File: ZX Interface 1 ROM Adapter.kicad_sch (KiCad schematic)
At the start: 4 parts, among them J1 Conn_01x08_Socket, J2 24DIL Socket, J3 Conn_01x16, J4 Conn_01x16

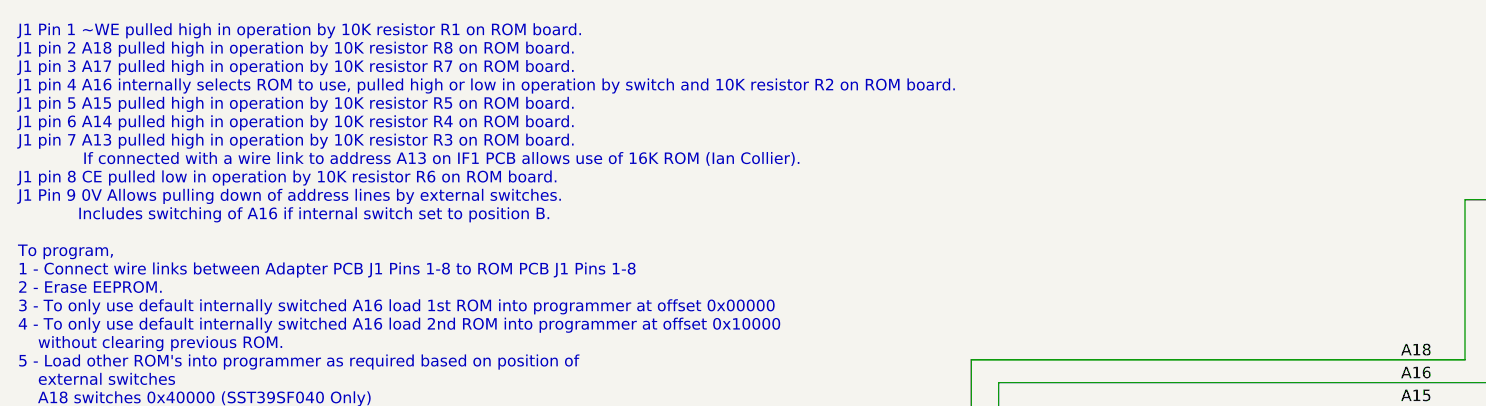
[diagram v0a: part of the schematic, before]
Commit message: Updated to use 8 Pin Right Angled Single-In-Line Connector
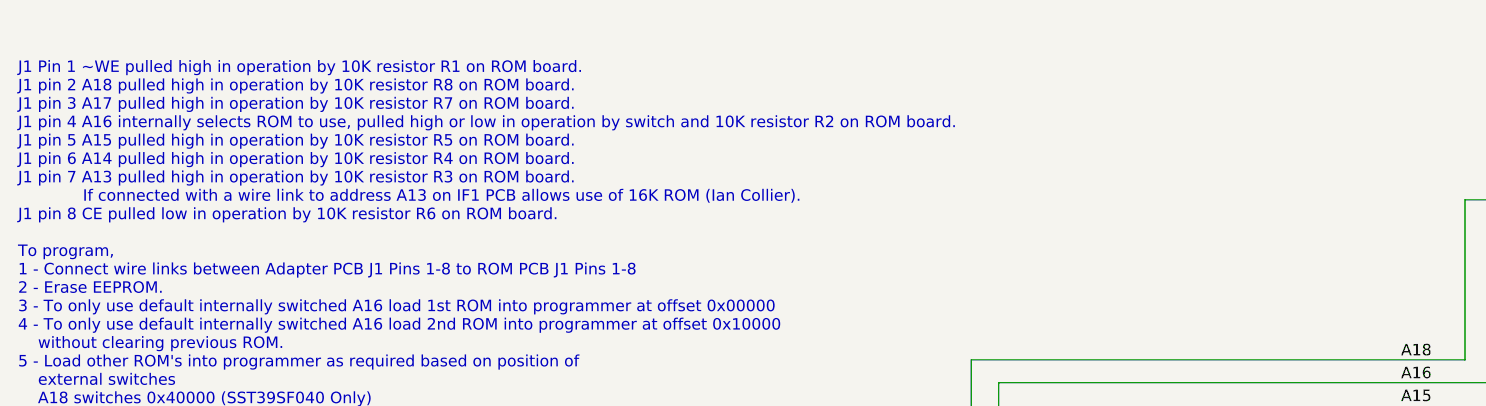
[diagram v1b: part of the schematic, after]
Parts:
- J1: footprint Connector_PinSocket_2.54mm:PinSocket_1x08_P2.54mm_Vertical -> Library:PinSocket_1x08_P2.54mm_HorizontalR
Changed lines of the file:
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@@
     (stroke (width 0) (type default))
   )
-  (text "J1 Pin 1 ~WE pulled high in operation by 10K resistor R1 on ROM board.\nJ1 pin 2 A18 pulled high in operation by 10K resistor R8 on ROM board.\nJ1 pin 3 A17 pulled high in operation by 10K resistor R7 on ROM board.\nJ1 pin 4 A16 internally selects ROM to use, pulled high or low in operation by switch and 10K resistor R2 on ROM board.\nJ1 pin 5 A15 pulled high in operation by 10K resistor R5 on ROM board.\nJ1 pin 6 A14 pulled high in operation by 10K resistor R4 on ROM board.\nJ1 pin 7 A13 pulled high in operation by 10K resistor R3 on ROM board. \n             If connected with a wire link to address A13 on IF1 PCB allows use of 16K ROM (Ian Collier).\nJ1 pin 8 CE pulled low in operation by 10K resistor R6 on ROM board.\nJ1 Pin 9 0V Allows pulling down of address lines by external switches.\n            Includes switching of A16 if internal switch set to position B.\n\nTo program,\n1 - Connect wire links between Adapter PCB J1 Pins 1-8 to ROM PCB J1 Pins 1-8  \n2 - Erase EEPROM.\n3 - To only use default internally switched A16 load 1st ROM into programmer at offset 0x00000\n4 - To only use default internally switched A16 load 2nd ROM into programmer at offset 0x10000\n    without clearing previous ROM.\n5 - Load other ROM's into programmer as required based on position of\n    external switches\n    A18 switches 0x40000 (SST39SF040 Only)\n    A17 switches 0x20000 (SST39SF020 and 040 Only)\n    A16 switches 0x10000 if internal switch set to position B.\n    A15 switches 0x08000\n    A14 switches 0x04000\n    A13 (DO NOT USE. Decoded by IF1 ULA)\n    A mix of switches is allowed and will increase the number of ROM positions\n    available, up to a maximum of 32.\n6 - program.\n\n"
+  (text "J1 Pin 1 ~WE pulled high in operation by 10K resistor R1 on ROM board.\nJ1 pin 2 A18 pulled high in operation by 10K resistor R8 on ROM board.\nJ1 pin 3 A17 pulled high in operation by 10K resistor R7 on ROM board.\nJ1 pin 4 A16 internally selects ROM to use, pulled high or low in operation by switch and 10K resistor R2 on ROM board.\nJ1 pin 5 A15 pulled high in operation by 10K resistor R5 on ROM board.\nJ1 pin 6 A14 pulled high in operation by 10K resistor R4 on ROM board.\nJ1 pin 7 A13 pulled high in operation by 10K resistor R3 on ROM board. \n             If connected with a wire link to address A13 on IF1 PCB allows use of 16K ROM (Ian Collier).\nJ1 pin 8 CE pulled low in operation by 10K resistor R6 on ROM board.\n\nTo program,\n1 - Connect wire links between Adapter PCB J1 Pins 1-8 to ROM PCB J1 Pins 1-8  \n2 - Erase EEPROM.\n3 - To only use default internally switched A16 load 1st ROM into programmer at offset 0x00000\n4 - To only use default internally switched A16 load 2nd ROM into programmer at offset 0x10000\n    without clearing previous ROM.\n5 - Load other ROM's into programmer as required based on position of\n    external switches\n    A18 switches 0x40000 (SST39SF040 Only)\n    A17 switches 0x20000 (SST39SF020 and 040 Only)\n    A16 switches 0x10000 if internal switch set to position B.\n    A15 switches 0x08000\n    A14 switches 0x04000\n    A13 (DO NOT USE. Decoded by IF1 ULA)\n    A mix of switches is allowed and will increase the number of ROM positions\n    available, up to a maximum of 32.\n6 - program.\n\n"
     (at 16.002 76.2 0)
     (effects (font (size 1.27 1.27)) (justify left bottom))
@@
       (effects (font (size 1.27 1.27)) hide)
     )
-    (property "Footprint" "Connector_PinSocket_2.54mm:PinSocket_1x08_P2.54mm_Vertical" (at 191.77 48.768 0)
+    (property "Footprint" "Library:PinSocket_1x08_P2.54mm_HorizontalR" (at 191.77 48.768 0)
       (effects (font (size 1.27 1.27)) hide)
     )

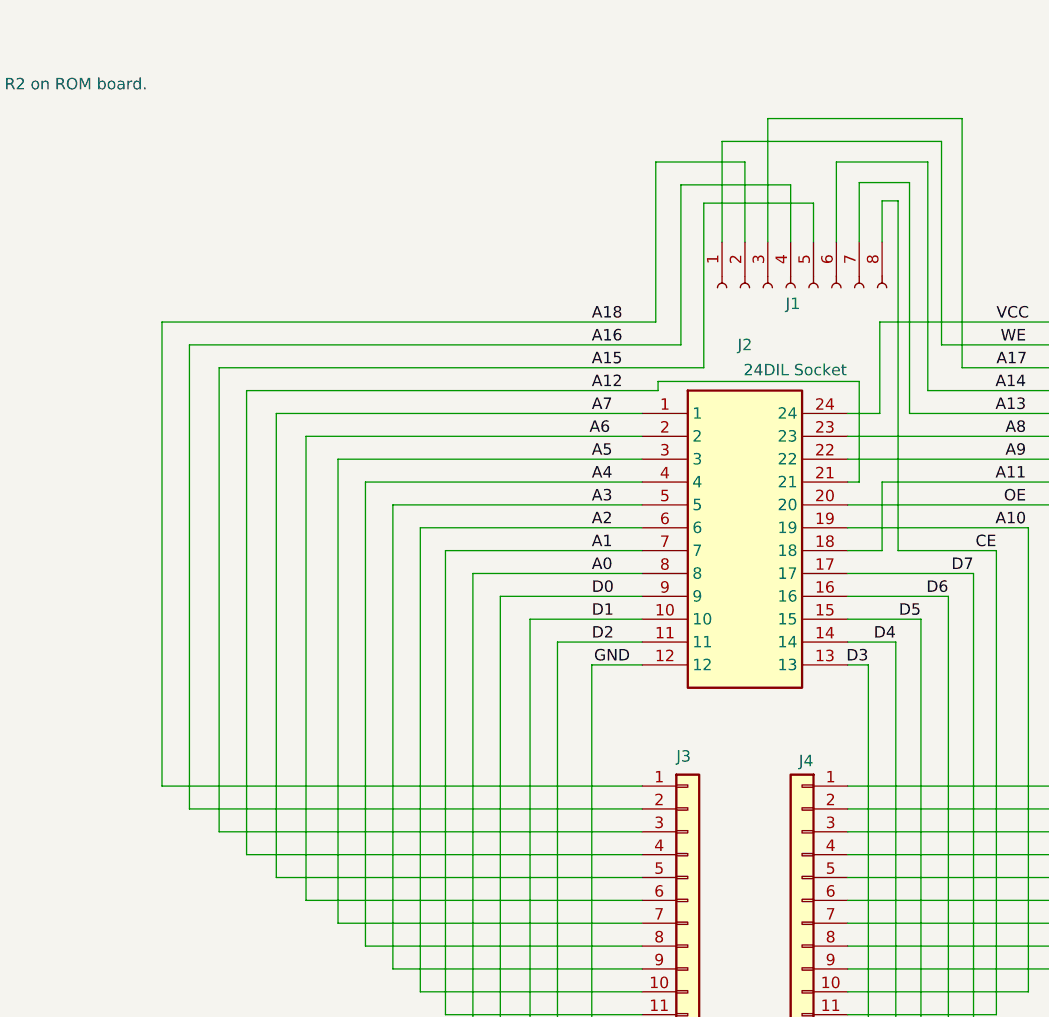
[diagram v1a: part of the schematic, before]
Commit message: Add files via upload
Updated to Kicad 9. Added ibom. Restructured folders.
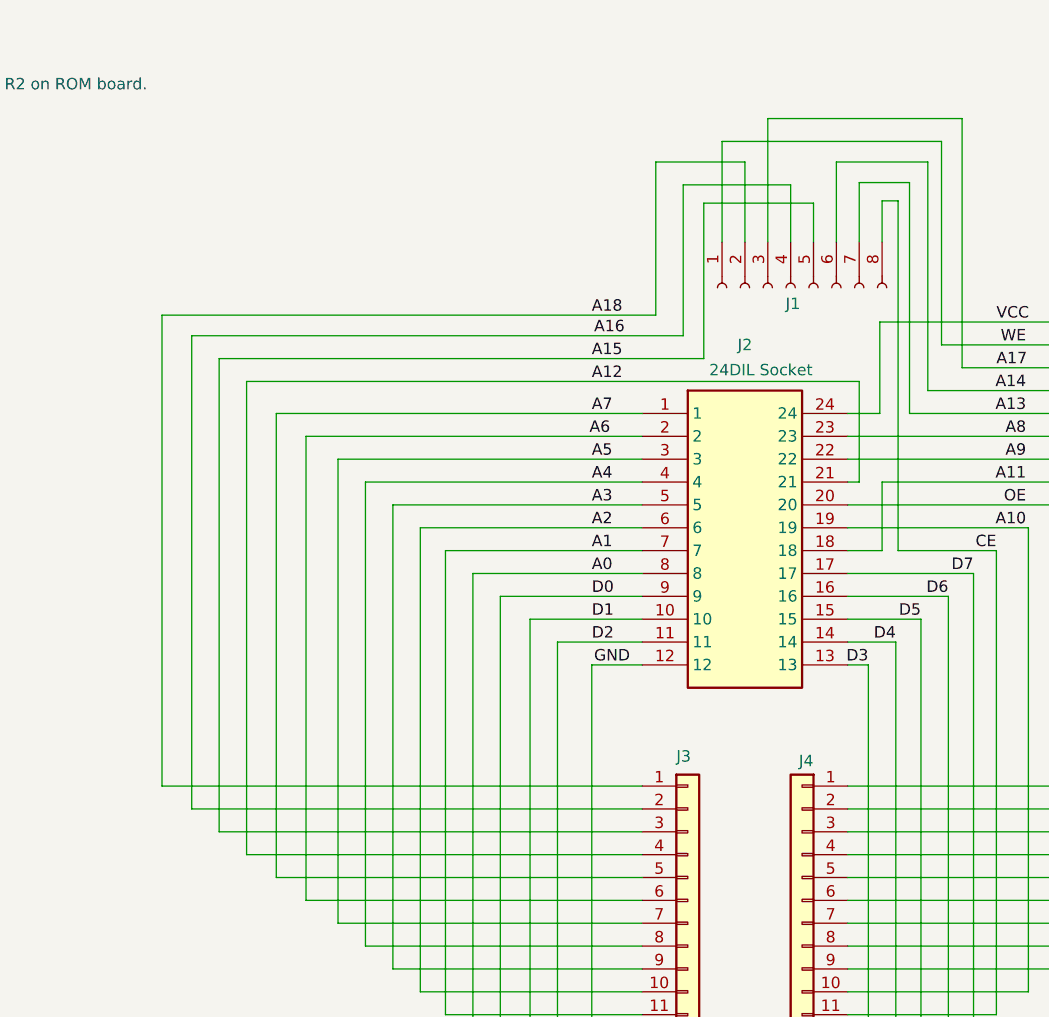
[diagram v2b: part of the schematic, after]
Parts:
- J1: footprint Library:PinSocket_1x08_P2.54mm_HorizontalR -> Mod:PinSocket_1x08_P2.54mm_HorizontalR; symbol Connector:Conn_01x08_Socket -> Prog_Adapter:Conn_01x08_Socket
- J2: footprint Package_DIP:DIP-24_W15.24mm_Socket_LongPads -> Mod:DIP-24_W15.24mm_Socket_LongPads; symbol DIL24:DILB24P-224TLF -> Prog_Adapter:DILB24P-224TLF
- J3, J4: footprint Connector_PinHeader_2.54mm:PinHeader_1x16_P2.54mm_Vertical -> Mod:PinHeader_1x16_P2.54mm_Vertical; symbol Connector_Generic:Conn_01x16 -> Prog_Adapter:Conn_01x16
